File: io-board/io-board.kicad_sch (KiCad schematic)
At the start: 0 parts

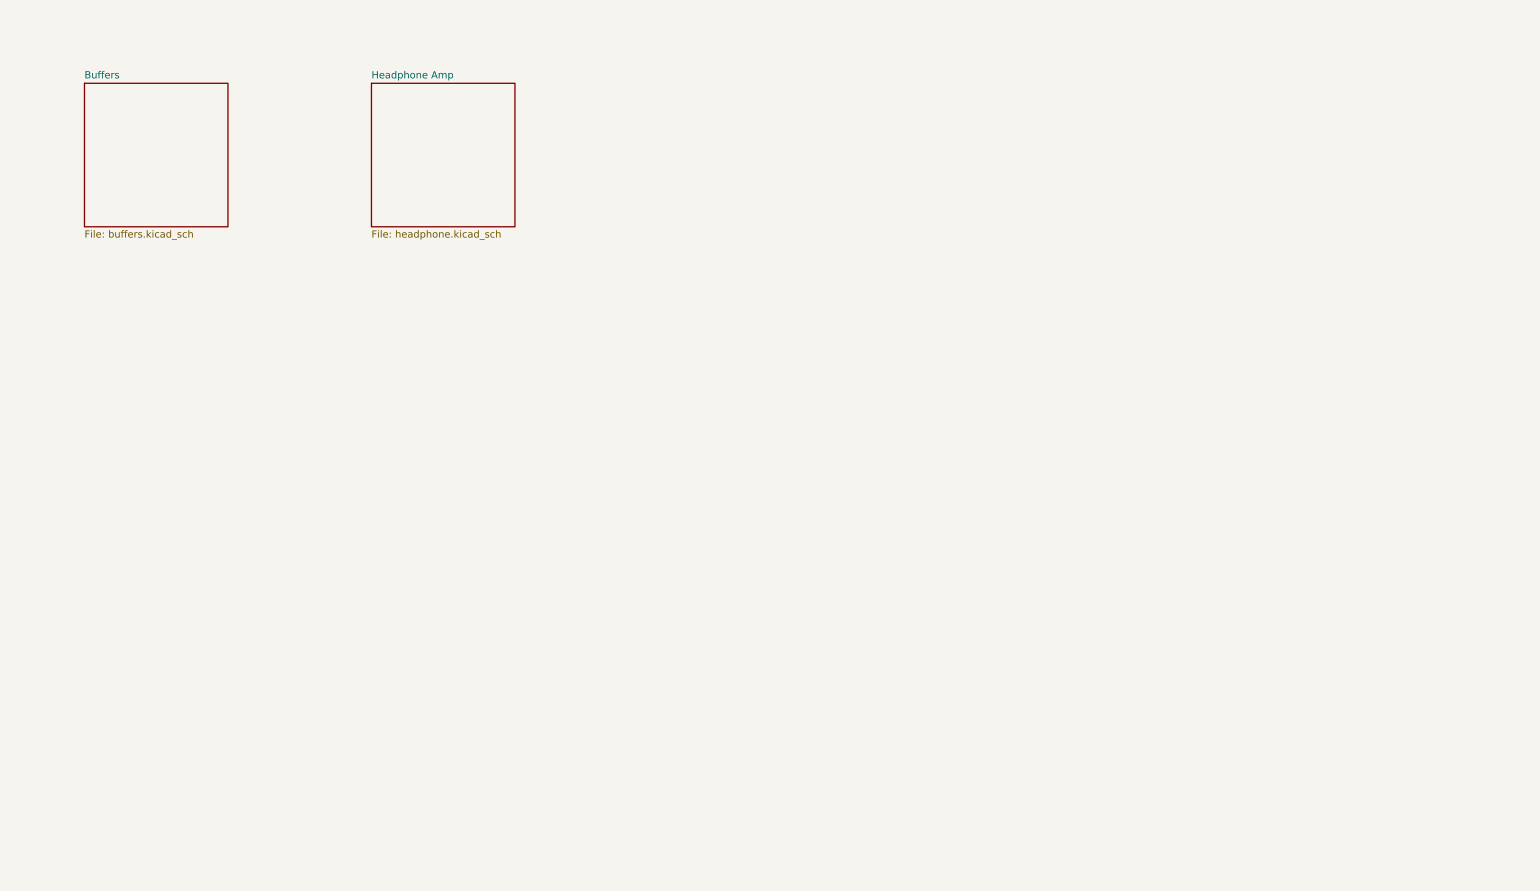
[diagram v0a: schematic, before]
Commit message: IO Board wip
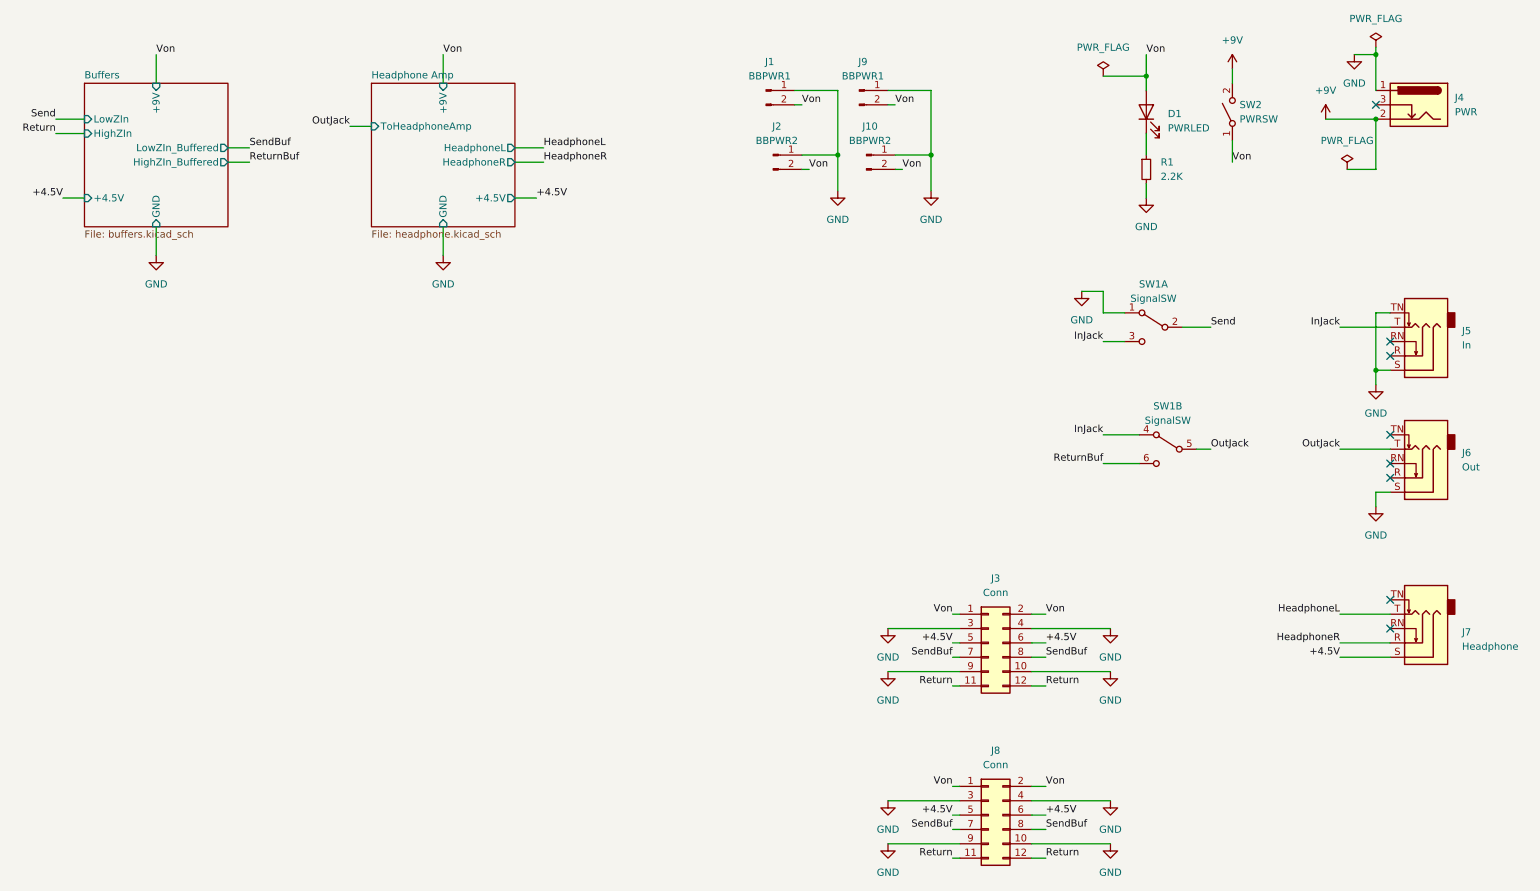
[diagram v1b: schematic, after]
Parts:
- added D1: PWRLED, LED_SMD:LED_0805_2012Metric_Pad1.15x1.40mm_HandSolder, symbol Device:LED
- added J1, J9: BBPWR1, Connector_PinHeader_2.54mm:PinHeader_1x02_P2.54mm_Vertical, symbol Connector:Conn_01x02_Male
- added J10, J2: BBPWR2, Connector_PinHeader_2.54mm:PinHeader_1x02_P2.54mm_Vertical, symbol Connector:Conn_01x02_Male
- added J3, J8: Conn, Connector_PinHeader_2.54mm:PinHeader_2x06_P2.54mm_Vertical, symbol Connector_Generic:Conn_02x06_Odd_Even
- added J4: PWR, Connector_BarrelJack:BarrelJack_GCT_DCJ200-10-A_Horizontal, symbol Connector:Barrel_Jack_Switch
- added J5: In, tayda-6mm35-jack-pcb-compact:tayda-6mm35-jack-pcb-compact, symbol Connector:AudioJack3_SwitchTR
- added J6: Out, tayda-6mm35-jack-pcb-compact:tayda-6mm35-jack-pcb-compact, symbol Connector:AudioJack3_SwitchTR
- added J7: Headphone, Connector_Audio:Jack_3.5mm_CUI_SJ1-3525N_Horizontal, symbol Connector:AudioJack3_SwitchTR
- added R1: 2.2K, Resistor_SMD:R_0603_1608Metric_Pad0.98x0.95mm_HandSolder, symbol Device:R_Small
- added SW1: SignalSW, switches:DPDT.LUGS, symbol Switch:SW_DPDT_x2
- added SW2: PWRSW, switches:SPDT.LUGS, symbol Switch:SW_SPST
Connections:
- new net: D1.1 (K), R1.1
- new net +4.5V: J3.5 (Pin_5), J3.6 (Pin_6), J7.S, J8.5 (Pin_5), J8.6 (Pin_6)
- new net +9V: J4.2, SW2.2 (B)
- new net GND: J1.1 (Pin_1), J10.1 (Pin_1), J2.1 (Pin_1), J3.10 (Pin_10), J3.3 (Pin_3), J3.4 (Pin_4), J3.9 (Pin_9), J4.1, J5.S, J5.TN, J6.S, J8.10 (Pin_10), J8.3 (Pin_3), J8.4 (Pin_4), J8.9 (Pin_9), J9.1 (Pin_1), R1.2, SW1.1 (A)
- new net HeadphoneL: J7.T
- new net HeadphoneR: J7.R
- new net InJack: J5.T, SW1.3 (C), SW1.4 (A)
- new net OutJack: J6.T, SW1.5 (B)
- new net Return: J3.11 (Pin_11), J3.12 (Pin_12), J8.11 (Pin_11), J8.12 (Pin_12)
- new net ReturnBuf: SW1.6 (C)
- new net Send: SW1.2 (B)
- new net SendBuf: J3.7 (Pin_7), J3.8 (Pin_8), J8.7 (Pin_7), J8.8 (Pin_8)
- new net Von: D1.2 (A), J1.2 (Pin_2), J10.2 (Pin_2), J2.2 (Pin_2), J3.1 (Pin_1), J3.2 (Pin_2), J8.1 (Pin_1), J8.2 (Pin_2), J9.2 (Pin_2), SW2.1 (A)
- no-connect marks 0 -> 8
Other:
- sheet Buffers ports: added +4.5V, +9V, GND, HighZIn, HighZIn_Buffered, LowZIn, LowZIn_Buffered; removed none
- sheet Headphone Amp ports: added +4.5V, +9V, GND, HeadphoneL, HeadphoneR, ToHeadphoneAmp; removed none

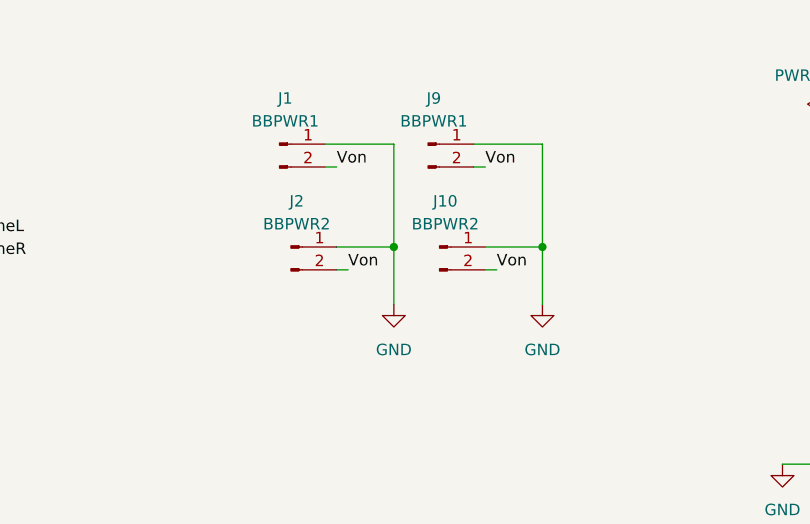
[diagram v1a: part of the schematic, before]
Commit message: Mounting holes
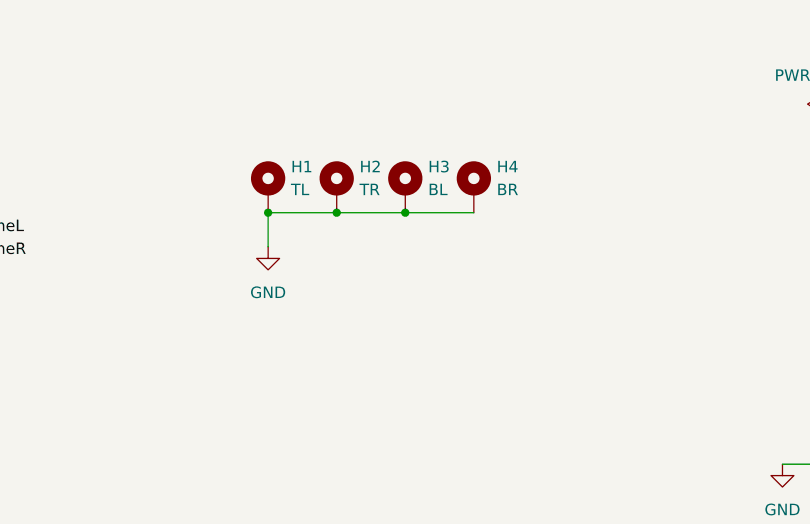
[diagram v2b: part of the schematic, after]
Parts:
- removed J1, J9: BBPWR1, Connector_PinHeader_2.54mm:PinHeader_1x02_P2.54mm_Vertical, symbol Connector:Conn_01x02_Male
- removed J10, J2: BBPWR2, Connector_PinHeader_2.54mm:PinHeader_1x02_P2.54mm_Vertical, symbol Connector:Conn_01x02_Male
- added H1: TL, MountingHole:MountingHole_3.2mm_M3_Pad_Via, symbol Mechanical:MountingHole_Pad
- added H2: TR, MountingHole:MountingHole_3.2mm_M3_Pad_Via, symbol Mechanical:MountingHole_Pad
- added H3: BL, MountingHole:MountingHole_3.2mm_M3_Pad_Via, symbol Mechanical:MountingHole_Pad
- added H4: BR, MountingHole:MountingHole_3.2mm_M3_Pad_Via, symbol Mechanical:MountingHole_Pad
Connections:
- net GND: now also H1.1, H2.1, H3.1, H4.1

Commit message: graphics
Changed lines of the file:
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@@
       (effects (font (size 1.27 1.27)) (justify left))
     )
-    (pin "LowZIn" input (at 25.4 31.75 180)
+    (pin "LowZIn" input (at 25.4 34.29 180)
       (effects (font (size 1.27 1.27)) (justify left))
     )
-    (pin "HighZIn" input (at 25.4 34.29 180)
+    (pin "HighZIn" input (at 25.4 31.75 180)
       (effects (font (size 1.27 1.27)) (justify left))
     )
-    (pin "HighZIn_Buffered" output (at 50.8 39.37 0)
+    (pin "HighZIn_Buffered" output (at 50.8 36.83 0)
       (effects (font (size 1.27 1.27)) (justify right))
     )
-    (pin "LowZIn_Buffered" output (at 50.8 36.83 0)
+    (pin "LowZIn_Buffered" output (at 50.8 39.37 0)
       (effects (font (size 1.27 1.27)) (justify right))
     )

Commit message: wip
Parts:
- D1: Mouser (none) -> 710-150080RS75000
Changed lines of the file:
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@@
+      (effects (font (size 1.27 1.27)) hide)
+    )
+    (property "Mouser" "710-150080RS75000" (id 4) (at 213.36 30.48 0)
       (effects (font (size 1.27 1.27)) hide)
     )

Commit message: wip
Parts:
- J7: Mouser (none) -> 490-SJ1-3525N
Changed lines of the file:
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@@
+      (effects (font (size 1.27 1.27)) hide)
+    )
+    (property "Mouser" "490-SJ1-3525N " (id 4) (at 261.62 124.46 0)
       (effects (font (size 1.27 1.27)) hide)
     )
@@
     )
     (path "/138f5238-2466-4b40-8443-8253ffd3dc8e/48760674-e7c2-41cd-9c9b-80f322666f85"
-      (reference "C10") (unit 1) (value "470u") (footprint "Capacitor_SMD:CP_Elec_4x5.4")
+      (reference "C10") (unit 1) (value "10u") (footprint "Capacitor_SMD:CP_Elec_4x5.4")
     )
     (path "/138f5238-2466-4b40-8443-8253ffd3dc8e/eeb9c945-6de0-4699-b432-001cf6c24a89"
@@
     )
     (path "/138f5238-2466-4b40-8443-8253ffd3dc8e/c7029152-01c8-4ab6-965a-087201f1072e"
-      (reference "R20") (unit 1) (value "1K") (footprint "Resistor_SMD:R_0603_1608Metric_Pad0.98x0.95mm_HandSolder")
+      (reference "R20") (unit 1) (value "1R") (footprint "Resistor_SMD:R_0603_1608Metric_Pad0.98x0.95mm_HandSolder")
     )
     (path "/138f5238-2466-4b40-8443-8253ffd3dc8e/ebcffb2b-e695-4589-90e7-a0bfbcb9e14d"
-      (reference "R21") (unit 1) (value "1K") (footprint "Resistor_SMD:R_0603_1608Metric_Pad0.98x0.95mm_HandSolder")
+      (reference "R21") (unit 1) (value "1R") (footprint "Resistor_SMD:R_0603_1608Metric_Pad0.98x0.95mm_HandSolder")
     )
     (path "/138f5238-2466-4b40-8443-8253ffd3dc8e/f498ffc9-0dac-45ce-b614-437eafc02c3d"
-      (reference "R22") (unit 1) (value "1K") (footprint "Resistor_SMD:R_0603_1608Metric_Pad0.98x0.95mm_HandSolder")
+      (reference "R22") (unit 1) (value "1R") (footprint "Resistor_SMD:R_0603_1608Metric_Pad0.98x0.95mm_HandSolder")
     )
     (path "/138f5238-2466-4b40-8443-8253ffd3dc8e/a0dc0a31-4783-48d5-bc69-693c2b4f62ae"
-      (reference "R23") (unit 1) (value "1K") (footprint "Resistor_SMD:R_0603_1608Metric_Pad0.98x0.95mm_HandSolder")
+      (reference "R23") (unit 1) (value "1R") (footprint "Resistor_SMD:R_0603_1608Metric_Pad0.98x0.95mm_HandSolder")
     )
     (path "/138f5238-2466-4b40-8443-8253ffd3dc8e/d1abd724-a11e-4d6a-80fb-85f9d7162352"

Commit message: io jlc part numbers
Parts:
- D1: LCSC (none) -> C84256
- R1: LCSC (none) -> C4190
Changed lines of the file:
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@@
+      (effects (font (size 1.27 1.27)) hide)
+    )
+    (property "LCSC" "C4190" (id 4) (at 213.36 40.64 0)
       (effects (font (size 1.27 1.27)) hide)
     )
@@
       (effects (font (size 1.27 1.27)) hide)
     )
+    (property "LCSC" "C84256" (id 5) (at 213.36 30.48 0)
+      (effects (font (size 1.27 1.27)) hide)
+    )

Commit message: Protato updates and schem
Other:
- company: (none) -> Andrei Salomatin / Pedal Markt
- title: (none) -> Protato
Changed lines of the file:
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@@
 (kicad_sch (version 20211123) (generator eeschema)
   (paper "A4")
+  (title_block
+    (title "Protato")
+    (rev "v1rev1")
+    (company "Andrei Salomatin / Pedal Markt")
+  )
   (junction (at 152.4 34.29) (diameter 0) (color 0 0 0 0)
   )
